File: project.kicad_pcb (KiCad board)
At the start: 2 copper layers, 0 parts

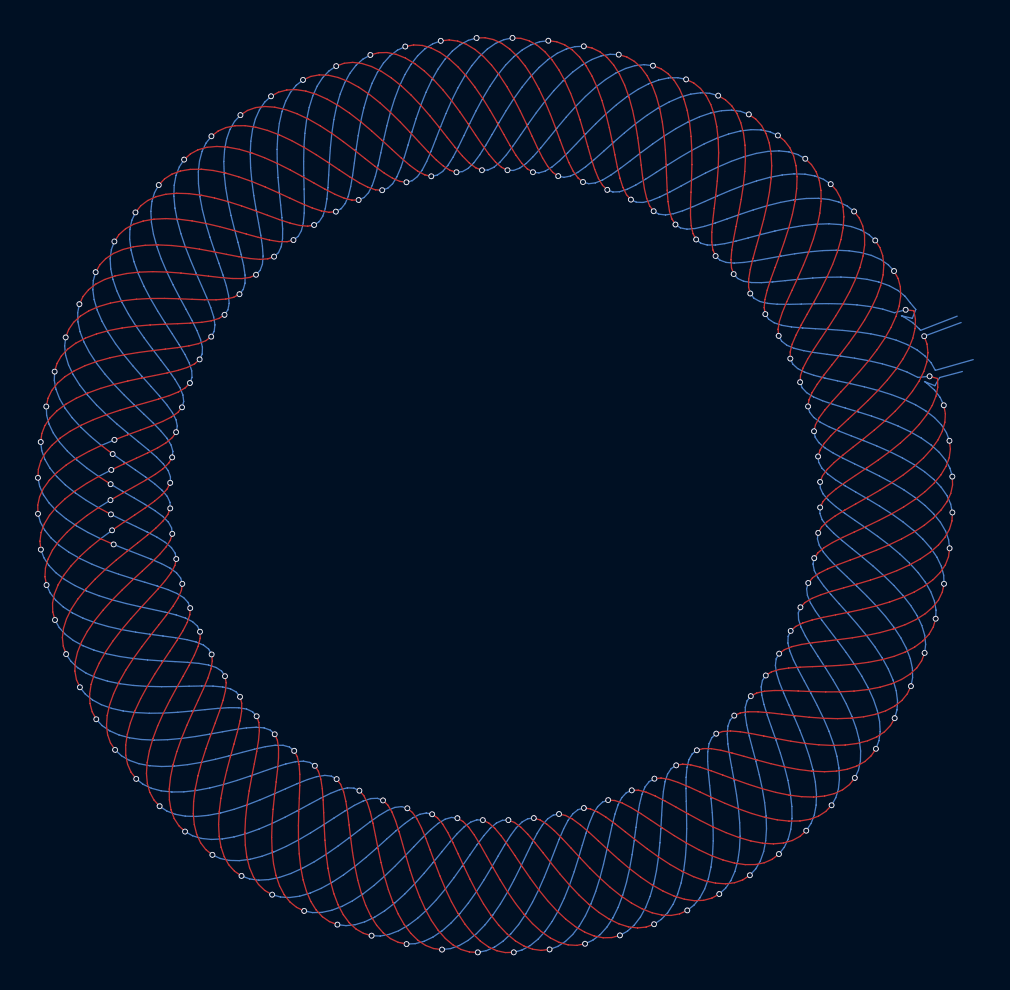
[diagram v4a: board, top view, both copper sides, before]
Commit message: Script now generates TX coils. the basic sensor generation is complete!
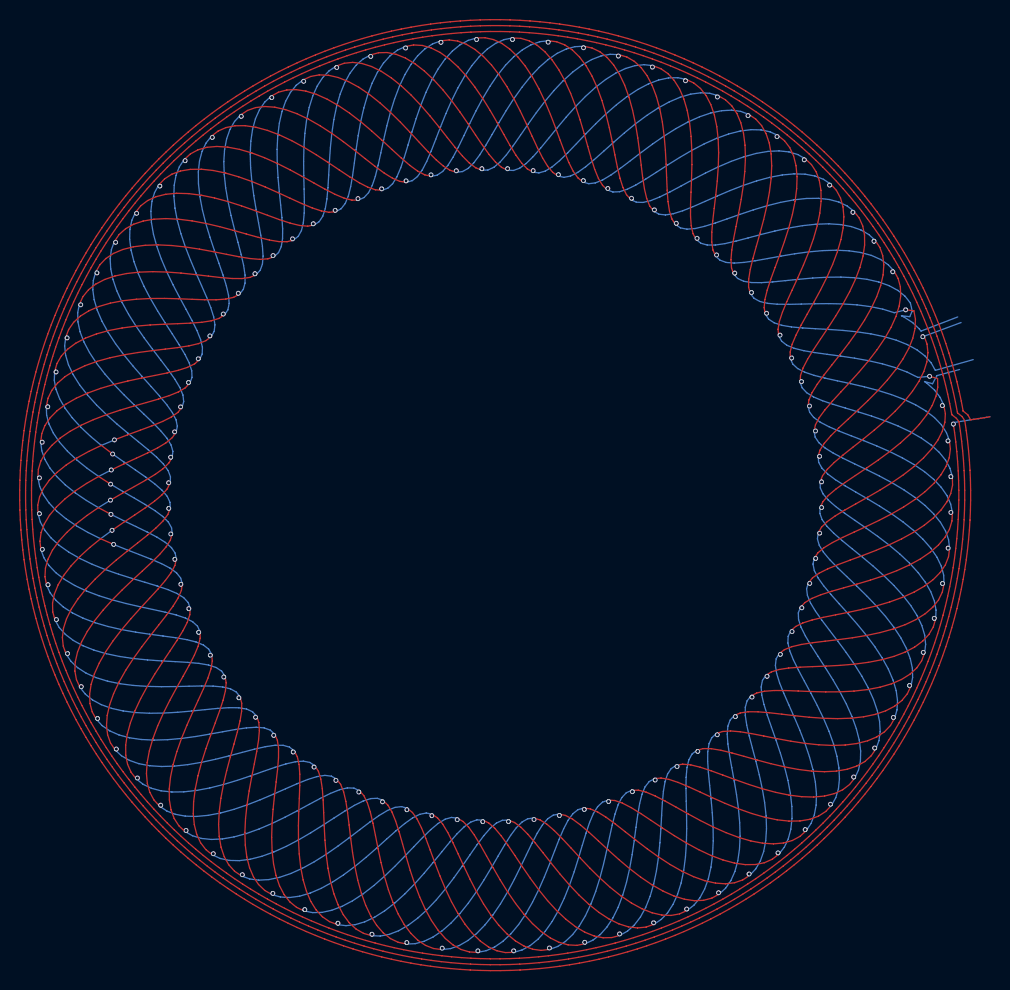
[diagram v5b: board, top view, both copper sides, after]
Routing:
- net 1: track 382.9 -> 1541.7 mm, vias 21 -> 84
- net 2: track 382.9 -> 1540.2 mm, vias 21 -> 84
- net TX: track 0.00 -> 905.5 mm, vias 0 -> 1
- net 4: track 393.6 -> 0.00 mm, vias 21 -> 0
- net 6: track 387.8 -> 0.00 mm, vias 21 -> 0
- net 5: track 386.9 -> 0.00 mm, vias 21 -> 0
- net 7: track 382.9 -> 0.00 mm, vias 21 -> 0
- net 8: track 382.9 -> 0.00 mm, vias 21 -> 0
- net 3: track 382.9 -> 0.00 mm, vias 21 -> 0
